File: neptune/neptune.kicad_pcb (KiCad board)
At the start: 4 copper layers, 39 x 67.2 mm, 71 parts, among them J1 Conn_Coaxial, J2 THD2528-11SD-GF, J3 USB_B_Micro, J4 Conn_01x02, J5 Conn_01x04, J6 Conn_01x04, J7 Conn_01x04, Q1 Si2301-TP, Q2 AO3401A, SW1 TS-1187A-B-A-B, SW2 TS-1187A-B-A-B, U1 ADR5040ARTZ-2.048, U2 LM393, U3 TPS54331D, U4 LP3993-33B3F, U5 RFM95W-915S2, U6 STM32F411RETx, U7 BMX055, U8 USBLC6-2SC6, Y1 12MHz, Y2 32.768k

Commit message: Updated some footprints, restarted routing
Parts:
- C15, C16, C17, C18: footprint Capacitor_SMD:C_0805_2012Metric -> Capacitor_SMD:C_0603_1608Metric
- D1, J2, Q1, R1, U5: moved to B.Cu
- J1: footprint Connector_Coaxial:SMA_Amphenol_132291_Vertical -> Connector_Coaxial:U.FL_Molex_MCRF_73412-0110_Vertical
- J5: footprint Connector_JST:JST_EH_B4B-EH-A_1x04_P2.50mm_Vertical -> Connector_PinHeader_2.54mm:PinHeader_1x04_P2.54mm_Vertical
- SW1, SW2: footprint Button_Switch_SMD:SW_Push_1P1T_NO_CK_KSC6xxJ -> Button_Switch_SMD:SW_Tactile_SPST_NO_Straight_CK_PTS636Sx25SMTRLFS
- TP1, TP2, TP3, TP4: footprint TestPoint:TestPoint_Pad_D2.0mm -> TestPoint:TestPoint_Pad_D1.0mm
- moved C1 155.7 mm to (209.6, 56.2)
- moved Q2 155.7 mm to (206.4, 62.2)
- moved R2 155.7 mm to (211.6, 56.0)
- moved R3 155.7 mm to (211.6, 57.2)
- moved R5 155.7 mm to (209.1, 61.5)
- moved U2 155.7 mm to (212.4, 61.7)
- moved R1 154.6 mm to (200.5, 81.8)
- moved Q1 153.0 mm to (201.8, 78.8), turned to -90 degrees
- moved D1 152.7 mm to (202.5, 75.8)
- moved R4 152.5 mm to (208.0, 65.2)
- moved C10 137.9 mm to (196.2, 51.3)
- moved C11 137.9 mm to (193.4, 57.8)
- moved C2 137.9 mm to (185.9, 46.5)
- moved C4 137.9 mm to (189.2, 45.5)
- moved C8 137.9 mm to (195.9, 47.5)
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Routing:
- net +5V: track 14.0 -> 0.00 mm
- net /Power/BATT: track 4.08 -> 0.00 mm
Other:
- board size 39 x 67.2 mm -> 182.4 x 134.5 mm

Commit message: Continued routing
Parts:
- removed J2: THD2528-11SD-GF, local-library:THD252811SDGF
- added U10: AT25SF081-XMHF-X, Package_SO:SOP-8_5.28x5.23mm_P1.27mm, F.Cu at (183.0, 120.2)
- C1, C10, C12, C13, C15, C16, C17, C18, C9, Q2, R2, R3, R4, R5, R7, U1, U2, U7: moved to B.Cu
- C11: footprint Capacitor_SMD:C_0805_2012Metric -> Capacitor_SMD:C_0603_1608Metric
- C2, C4: footprint Capacitor_SMD:C_0805_2012Metric_Pad1.18x1.45mm_HandSolder -> Capacitor_SMD:C_0603_1608Metric
- L2: footprint Inductor_SMD:L_0805_2012Metric -> Inductor_SMD:L_0603_1608Metric
- moved C17 133.5 mm to (195.5, 127.0), turned to 0 degrees
- moved C16 133.3 mm to (195.2, 129.2)
- moved Y1 128.4 mm to (194.0, 126.0), turned to 0 degrees
- moved Y2 128.4 mm to (194.0, 129.2), turned to 0 degrees
- moved H3 126.0 mm to (205.5, 133.5)
- moved C18 123.5 mm to (192.8, 129.2), turned to 90 degrees
- moved C15 122.9 mm to (192.5, 127.0), turned to 180 degrees
- moved H2 120.8 mm to (205.5, 86.5)
- moved SW2 117.0 mm to (203.2, 127.2), turned to 180 degrees
- moved C3 112.6 mm to (148.0, 113.7)
- moved C5 112.6 mm to (148.0, 116.2)
- moved C7 112.6 mm to (148.0, 118.8)
- moved J1 111.5 mm to (182.8, 113.0), turned to 180 degrees
- moved J4 104.1 mm to (194.0, 89.5)
- moved J7 102.5 mm to (189.5, 132.7)
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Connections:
- C12 pad 1: +3.3V -> +3V3
- C13 pad 1: +3.3V -> +3V3
- U5 pad 13: +3.3V -> +3V3
- U6 pad 10: unconnected-(U6-PC2-Pad10) -> /STM32/IMU_MISO
- U6 pad 11: /Data management/CS_SD -> /STM32/IMU_MOSI
- U6 pad 21: /STM32/IMU_SCK -> unconnected-(U6-PA5-Pad21)
- U6 pad 22: /STM32/IMU_MISO -> unconnected-(U6-PA6-Pad22)
- U6 pad 23: /STM32/IMU_MOSI -> unconnected-(U6-PA7-Pad23)
- U6 pad 26: /STM32/CE_ACC -> unconnected-(U6-PB0-Pad26)
- U6 pad 27: /STM32/CE_GYR -> unconnected-(U6-PB1-Pad27)
- U6 pad 28: /STM32/CE_MAG -> unconnected-(U6-PB2-Pad28)
- U6 pad 29: unconnected-(U6-PB10-Pad29) -> /STM32/IMU_SCK
- U6 pad 51: /Data management/CLK_SD -> /Data management/SCK_FC
- U6 pad 52: /Data management/MISO_SD -> /Data management/MISO_FC
- U6 pad 53: /Data management/MOSI_SD -> /Data management/MOSI_FC
- U6 pad 54: unconnected-(U6-PD2-Pad54) -> /STM32/CE_MAG
- U6 pad 55: unconnected-(U6-PB3-Pad55) -> /STM32/CE_GYR
- U6 pad 58: unconnected-(U6-PB6-Pad58) -> /STM32/CE_ACC
- U6 pad 59: unconnected-(U6-PB7-Pad59) -> /Data management/WP_FC
- U6 pad 61: unconnected-(U6-PB8-Pad61) -> /Data management/HOLD_FC
- U6 pad 62: unconnected-(U6-PB9-Pad62) -> /Data management/CS_FC
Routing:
- net +3V3: track 0.00 -> 36.1 mm, vias 0 -> 9
- net /STM32/IMU_SCK: track 0.00 -> 27.7 mm, vias 0 -> 2
- net /Data management/MISO_RF: track 0.00 -> 21.2 mm, vias 0 -> 1
- net /STM32/CE_ACC: track 0.00 -> 20.8 mm, vias 0 -> 2
- net /STM32/S2_feedback: track 0.00 -> 20.6 mm, vias 0 -> 2
- net /STM32/IMU_MOSI: track 0.00 -> 20.0 mm, vias 0 -> 1
- net /STM32/CE_MAG: track 0.00 -> 19.5 mm, vias 0 -> 2
- net /STM32/CE_GYR: track 0.00 -> 19.2 mm, vias 0 -> 2
- net /Data management/SCK_RF: track 0.00 -> 19.1 mm, vias 0 -> 1
- net /STM32/IMU_MISO: track 0.00 -> 19.1 mm, vias 0 -> 1
- net /Data management/MOSI_RF: track 0.00 -> 19.0 mm, vias 0 -> 1
- net /STM32/S1_control: track 0.00 -> 18.2 mm, vias 0 -> 2
- net /STM32/S1_feedback: track 0.00 -> 17.3 mm
- net Net-(U3-VSENSE): track 3.60 -> 20.8 mm, vias 0 -> 2
- net /STM32/OSC32_OUT: track 0.00 -> 16.1 mm, vias 0 -> 2
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- added copper zone on In1.Cu, net +3V3
- added copper zone on B.Cu, net GND
- removed copper zone on F.Cu, net (none)
- removed copper zone on F.Cu, net VCC
- removed copper zone on F.Cu, net VDC
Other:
- board size 182.4 x 134.5 mm -> 28 x 52 mm

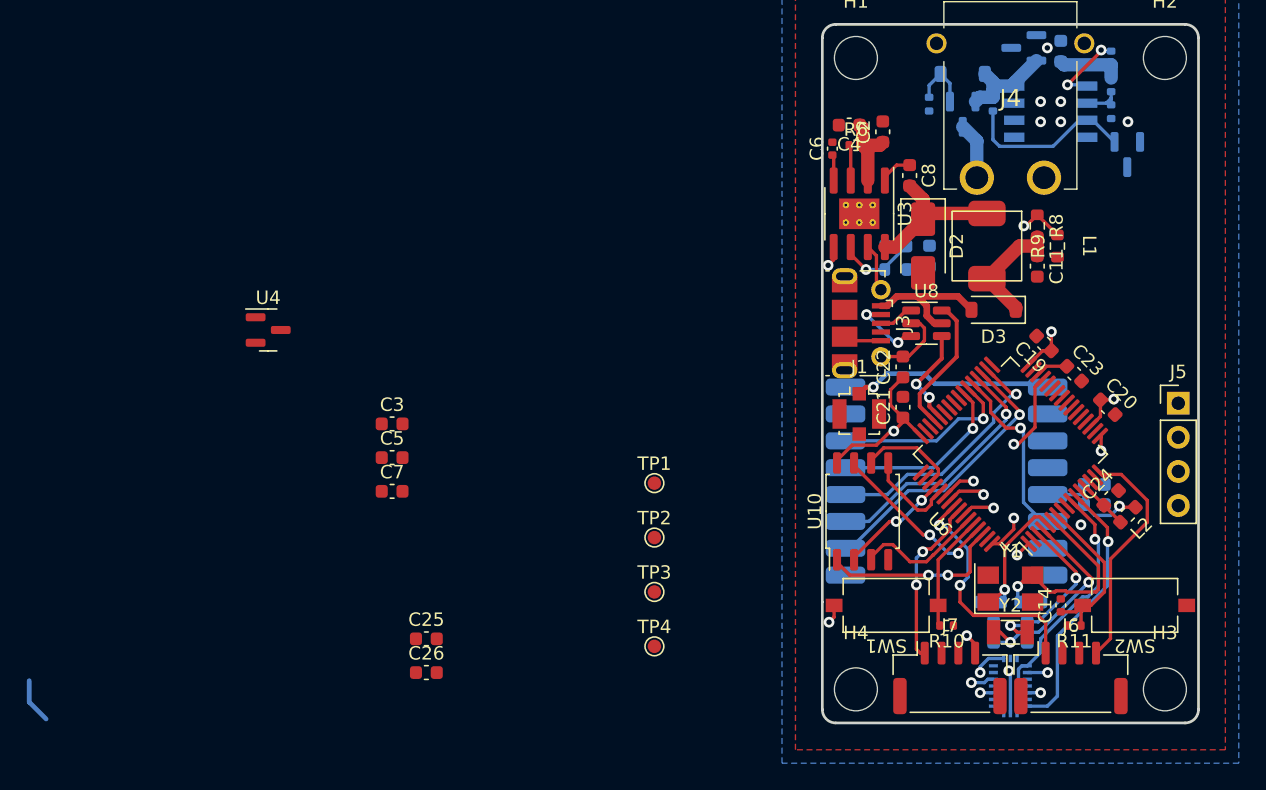
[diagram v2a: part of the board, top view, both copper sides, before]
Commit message: Routed 3.3V stepdown, added indicator LEDs
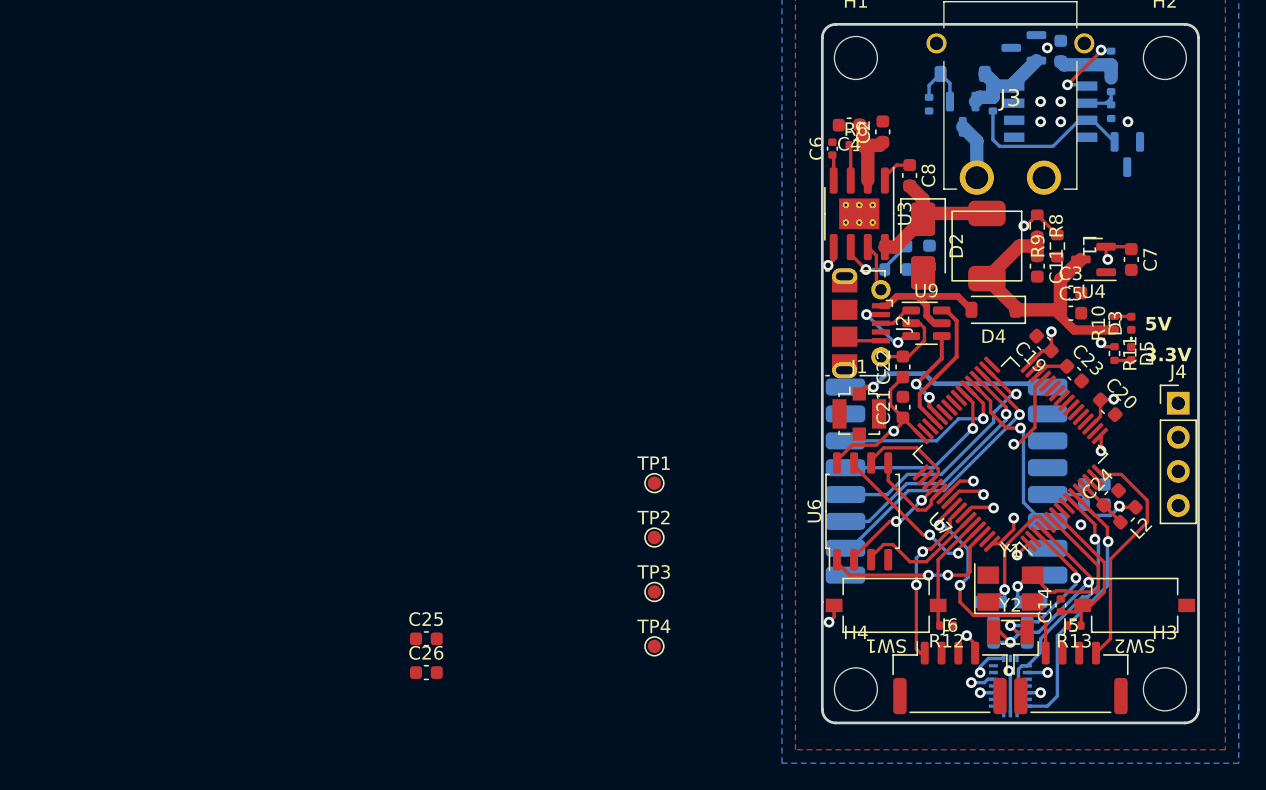
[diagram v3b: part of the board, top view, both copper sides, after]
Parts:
- added D3: LED, LED_SMD:LED_0402_1005Metric, F.Cu at (203.0, 106.2)
- added D5: LED, LED_SMD:LED_0402_1005Metric, F.Cu at (203.0, 108.5)
- added R10: 200, Resistor_SMD:R_0402_1005Metric, F.Cu at (201.8, 106.2)
- added R11: 200, Resistor_SMD:R_0402_1005Metric, F.Cu at (201.8, 108.5)
- moved U4 61.7 mm to (200.2, 101.5), turned to 180 degrees
- moved C7 57.7 mm to (203.0, 101.5), turned to -90 degrees
- moved C5 51.7 mm to (198.5, 105.5)
- moved C3 51.5 mm to (198.5, 104.0)
- renumbered D3 to D4, J3 to J2, J4 to J3, J5 to J4, J6 to J5, J7 to J6, R10 to R12, R11 to R13, U10 to U6, U6 to U7, U7 to U8, U8 to U9
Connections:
- C7 pad 1: +3.3V -> +3V3
- U4 pad 2: +3.3V -> +3V3
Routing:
- net +5V: track 9.37 -> 22.1 mm
- net +3V3: track 36.1 -> 40.2 mm, vias 9 -> 11
- net /STM32/USB_D+: track 13.9 -> 10.6 mm
- net Net-(D5-A): track 0.00 -> 1.26 mm
- net Net-(D3-A): track 0.00 -> 1.26 mm
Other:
- board text added: "3.3V"
- board text added: "5V"

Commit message: Finished routing
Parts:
- C25, C26: moved to B.Cu
- moved C25 47.1 mm to (197.5, 133.8)
- moved TP4 42.6 mm to (203.8, 108.0)
- moved TP3 39.8 mm to (203.8, 109.8)
- moved TP2 39.6 mm to (203.8, 106.2)
- moved C26 39.2 mm to (189.8, 133.0), turned to 180 degrees
- moved TP1 38.8 mm to (203.8, 104.2)
- moved D3 0.75 mm to (202.2, 106.2)
- moved D5 0.75 mm to (202.2, 108.5)
- moved R10 0.75 mm to (201.0, 106.2)
- moved R11 0.75 mm to (201.0, 108.5)
- moved C18 0.25 mm to (192.5, 129.2)
- renumbered D4 to D3, J2 to J3, J3 to J4, J4 to J5, J5 to J6, J6 to J7, R12 to R10, R13 to R11, U6 to U10, U7 to U6, U8 to U7, U9 to U8
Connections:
- TP4 pad 1: +3.3V -> +3V3
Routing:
- net +5V: track 22.1 -> 80.0 mm, vias 0 -> 3
- net /STM32/SWCLK: track 0.00 -> 23.8 mm, vias 0 -> 1
- net /STM32/SWDIO: track 0.00 -> 19.8 mm, vias 0 -> 1
- net +3V3: track 40.2 -> 55.3 mm
- net VBUS: track 10.5 -> 24.4 mm, vias 0 -> 2
- net VCC: track 5.96 -> 18.4 mm, vias 0 -> 1
- net GND: track 12.2 -> 20.8 mm, vias 7 -> 17
- net Net-(Q2-G): track 5.91 -> 10.9 mm, vias 2 -> 3
- net /STM32/IMU_MOSI: track 20.0 -> 23.4 mm
- net VDC: track 13.0 -> 15.0 mm
- net /STM32/S1_feedback: track 17.3 -> 19.0 mm
- net /STM32/S1_control: track 18.2 -> 19.4 mm
- net /STM32/OSC_IN: track 10.2 -> 11.3 mm
- net /STM32/OSC32_OUT: track 16.1 -> 16.7 mm
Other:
- board text added: "GND"
- board text added: "VBUS"

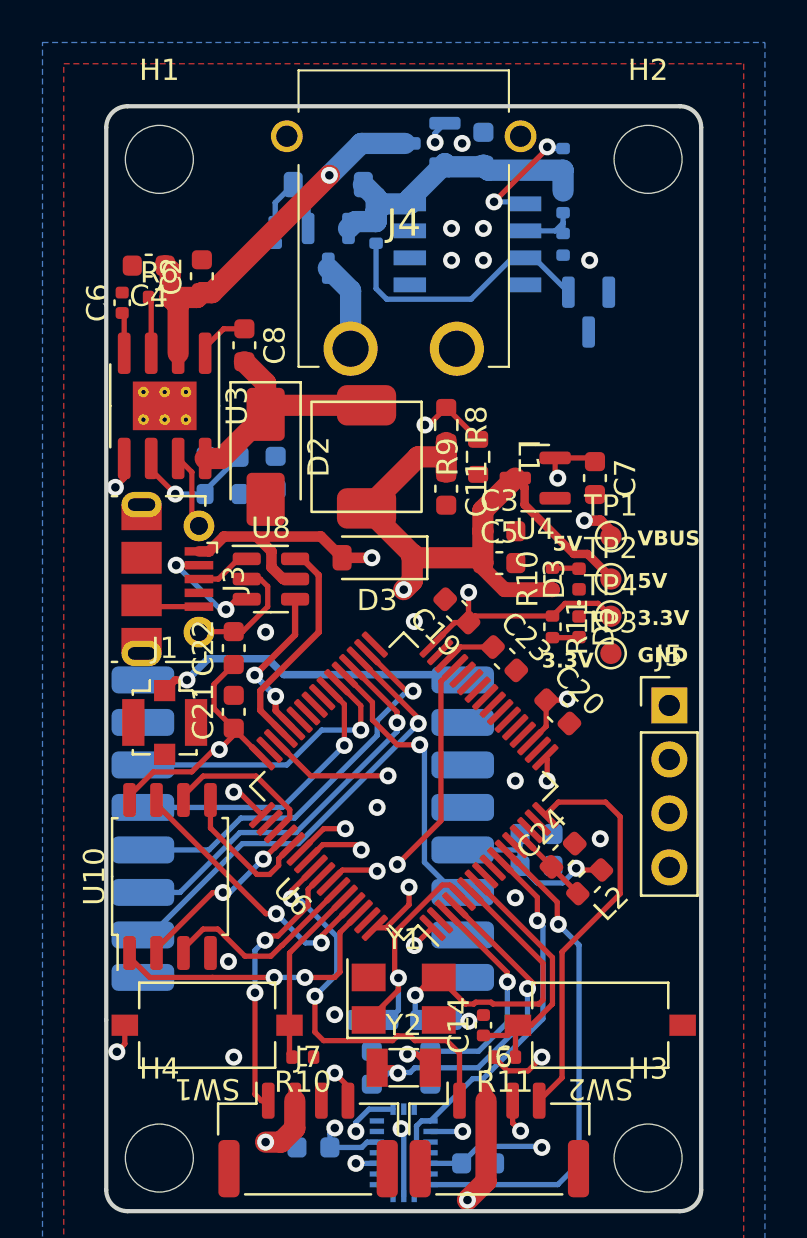
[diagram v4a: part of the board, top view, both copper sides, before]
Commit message: Moved USB slightly, added 3D models
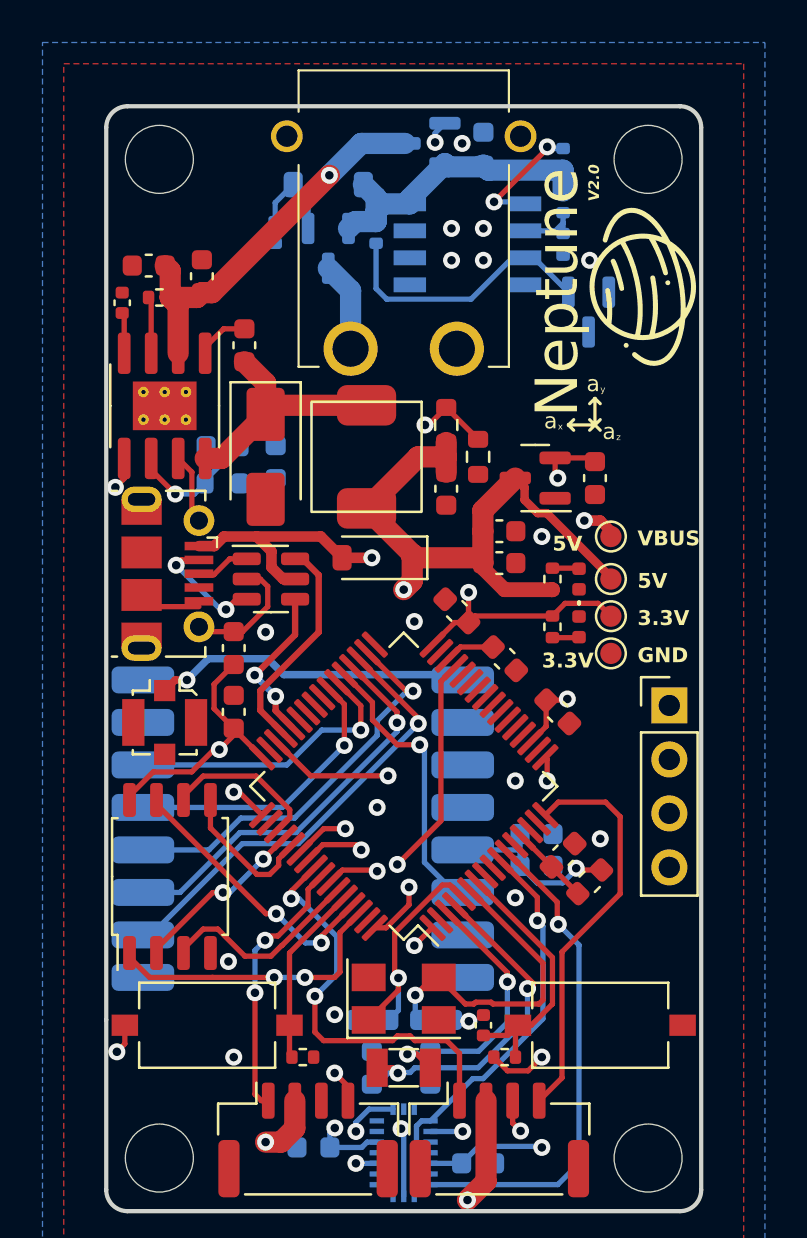
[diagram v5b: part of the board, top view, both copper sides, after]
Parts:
- added G***: LOGO, local-library:neptune_outline, F.Cu at (205.2, 92.5)
- added G***: LOGO, local-library:HPR_Logo, B.Cu at (200.5, 104.0)
- moved C10 0.50 mm to (185.5, 100.0)
- moved C9 0.50 mm to (188.0, 100.8)
- moved R7 0.50 mm to (185.5, 101.8)
- moved J3 0.25 mm to (182.9, 106.0)
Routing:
- net VBUS: track 24.4 -> 25.0 mm
- net GND: track 20.8 -> 20.6 mm, vias 17 -> 18
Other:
- board text added: "Designed by Jack Bradley"
- board text added: "Neptune"
- board text added: "V2.0"
- board text added: "a"
- board text added: "x"
- board text added: "y"
- board text added: "z"

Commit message: Small change
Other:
- board text added: "CLK"
- board text added: "IO"
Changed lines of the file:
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@@
     (effects (font (size 0.75 0.75) (thickness 0.15)) (justify left bottom))
+  )
+  (gr_text "CLK" (at 205 120.5 90) (layer "F.SilkS")
+    (effects (font (size 0.5 0.5) (thickness 0.1) bold) (justify left bottom))
   )
   (gr_text "z" (at 204 99.75) (layer "F.SilkS")
@@
     (effects (font (size 0.7 0.7) (thickness 0.175) bold) (justify left bottom))
   )
-  (gr_text "3.3V" (at 200.5 110.5) (layer "F.SilkS")
-    (effects (font (size 0.7 0.7) (thickness 0.175) bold) (justify left bottom))
+  (gr_text "3.3V" (at 205 113 90) (layer "F.SilkS")
+    (effects (font (size 0.5 0.5) (thickness 0.1) bold) (justify left bottom))
   )
   (gr_text "3.3V" (at 205 108.5) (layer "F.SilkS")
@@
     (effects (font (size 0.3 0.3) (thickness 0.075)) (justify left bottom))
   )
-  (gr_text "5V" (at 201 105) (layer "F.SilkS")
-    (effects (font (size 0.7 0.7) (thickness 0.175) bold) (justify left bottom))
+  (gr_text "GND" (at 205 115.5 90) (layer "F.SilkS")
+    (effects (font (size 0.5 0.5) (thickness 0.1) bold) (justify left bottom))
+  )
+  (gr_text "IO" (at 205 117.6 90) (layer "F.SilkS")
+    (effects (font (size 0.5 0.5) (thickness 0.1) bold) (justify left bottom))
   )
   (gr_text "a" (at 200.6 99.25) (layer "F.SilkS")
